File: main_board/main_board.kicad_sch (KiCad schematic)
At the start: 74 parts, among them J2 Conn_01x02, J3 Conn_01x02, J4 EncSide, J5 MainSide, J6 EncSide, J7 MainSide, Q1 ST-1KL3A, Q2 ST-1KL3A, Q3 ST-1KL3A, Q4 ST-1KL3A, Q5 IRLML6344, Q6 IRLML6344, Q7 IRLML6344, Q8 IRLML6344, U1 ADCS7476, U10 AS5047D, U11 LSM6DSR, U2 BD63573NUV, U3 ADCS7476, U4 ADCS7476, U5 BD63573NUV, U6 ESP32-S3-PICO-1-N8R2, U7 AS5047D, U8 ADCS7476, U9 ADCS7476

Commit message: アートワーク : 部品配置
Signed-off-by: Kazuki Iida <elkel53930@gmail.com>
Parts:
- D4, D5: footprint Library:SFH4550 -> Library:SFH4550_Mirror
- Q1, Q2: footprint Library:ST-1KL3A -> Library:ST-1KL3A_Mirror
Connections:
- net CS_ENC_L: now also U6.40 (GPIO35); no longer U6.24 (GPIO18)
- net CS_ENC_R: now also U6.41 (GPIO36); no longer U6.25 (GPIO19)
- net CWCCW_L: now also U6.39 (GPIO34); no longer U6.40 (GPIO35)
- net CWCCW_R: now also U6.43 (GPIO38); no longer U6.42 (GPIO37)
- net LED_0: now also R1.1; no longer R1.2
- net LED_1: now also U6.24 (GPIO18); no longer U6.38 (GPIO33)
- net PWM_L: now also U6.38 (GPIO33); no longer U6.39 (GPIO34)
- net PWM_R: now also U6.42 (GPIO37); no longer U6.41 (GPIO36)
- net at D1.1 (K): now also R1.2; no longer R1.1
- net RXD renamed RXD0
- net TXD renamed TXD0
- no-connect marks 35 -> 38
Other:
- moved on the sheet: R1
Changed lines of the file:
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@@
 	)
 	(no_connect
+		(at 218.44 99.06)
+	)
+	(no_connect
 		(at 379.73 171.45)
 	)
@@
 	)
 	(no_connect
+		(at 233.68 154.94)
+	)
+	(no_connect
 		(at 379.73 203.2)
 	)
@@
 	)
 	(no_connect
+		(at 223.52 154.94)
+	)
+	(no_connect
 		(at 220.98 154.94)
 	)
@@
 	(wire
 		(pts
-			(xy 218.44 83.82) (xy 218.44 99.06)
-		)
-		(stroke
-			(width 0)
-			(type default)
-		)
-	)
-	(wire
-		(pts
 			(xy 85.09 172.72) (xy 96.52 172.72)
 		)
@@
 	(wire
 		(pts
+			(xy 171.45 118.11) (xy 185.42 118.11)
+		)
+		(stroke
+			(width 0)
+			(type default)
+		)
+	)
+	(wire
+		(pts
 			(xy 226.06 255.27) (xy 226.06 252.73)
 		)
@@
 	(wire
 		(pts
-			(xy 231.14 154.94) (xy 231.14 170.18)
-		)
-		(stroke
-			(width 0)
-			(type default)
-		)
-	)
-	(wire
-		(pts
 			(xy 45.72 107.95) (xy 49.53 107.95)
 		)
@@
 	(wire
 		(pts
+			(xy 238.76 83.82) (xy 238.76 99.06)
+		)
+		(stroke
+			(width 0)
+			(type default)
+		)
+	)
+	(wire
+		(pts
 			(xy 68.58 149.86) (xy 60.96 149.86)
 		)
@@
 	(wire
 		(pts
-			(xy 115.57 96.52) (xy 115.57 92.71)
+			(xy 171.45 120.65) (xy 194.31 120.65)
 		)
 		(stroke
@@
 	(wire
 		(pts
-			(xy 179.07 120.65) (xy 194.31 120.65)
+			(xy 115.57 96.52) (xy 115.57 92.71)
 		)
 		(stroke
@@
 	(wire
 		(pts
-			(xy 179.07 118.11) (xy 185.42 118.11)
-		)
-		(stroke
-			(width 0)
-			(type default)
-		)
-	)
-	(wire
-		(pts
 			(xy 322.58 125.73) (xy 325.12 125.73)
 		)
@@
 	(wire
 		(pts
-			(xy 233.68 154.94) (xy 233.68 170.18)
-		)
-		(stroke
-			(width 0)
-			(type default)
-		)
-	)
-	(wire
-		(pts
 			(xy 250.19 115.57) (xy 265.43 115.57)
 		)
@@
 		)
 	)
-	(label "CHIP_PU"
-		(at 179.07 118.11 180)
-		(effects
-			(font
-				(size 1.27 1.27)
-			)
-			(justify right bottom)
-		)
-	)
 	(label "CS_RS"
 		(at 179.07 125.73 180)
@@
 	)
 	(label "CS_ENC_L"
-		(at 228.6 170.18 270)
+		(at 265.43 115.57 0)
 		(effects
 			(font
 				(size 1.27 1.27)
 			)
-			(justify right bottom)
+			(justify left bottom)
 		)
 	)
@@
 		)
 	)
-	(label "TXD"
-		(at 223.52 83.82 90)
-		(effects
-			(font
-				(size 1.27 1.27)
-			)
-			(justify left bottom)
-		)
-	)
 	(label "CS_IMU"
 		(at 226.06 219.71 90)
@@
 		)
 	)
-	(label "RXD"
-		(at 220.98 83.82 90)
-		(effects
-			(font
-				(size 1.27 1.27)
-			)
-			(justify left bottom)
-		)
-	)
 	(label "PWM_R"
-		(at 265.43 113.03 0)
+		(at 265.43 110.49 0)
 		(effects
 			(font
@@
 	)
 	(label "LED_1"
-		(at 265.43 120.65 0)
+		(at 228.6 170.18 270)
 		(effects
 			(font
 				(size 1.27 1.27)
 			)
-			(justify left bottom)
+			(justify right bottom)
 		)
 	)
@@
 	)
 	(label "CS_ENC_R"
-		(at 231.14 170.18 270)
+		(at 265.43 113.03 0)
 		(effects
 			(font
 				(size 1.27 1.27)
 			)
-			(justify right bottom)
+			(justify left bottom)
 		)
 	)
@@
 	)
 	(label "PWM_L"
-		(at 265.43 118.11 0)
+		(at 265.43 120.65 0)
 		(effects
 			(font
@@
 	)
 	(label "CWCCW_L"
-		(at 265.43 115.57 0)
+		(at 265.43 118.11 0)
 		(effects
 			(font
@@
 	)
 	(label "CWCCW_R"
-		(at 265.43 110.49 0)
+		(at 238.76 83.82 90)
 		(effects
 			(font
@@
 		)
 	)
-	(label "GPIO0"
-		(at 179.07 120.65 180)
-		(effects
-			(font
-				(size 1.27 1.27)
-			)
-			(justify right bottom)
-		)
-	)
 	(label "PWM_R"
 		(at 314.96 72.39 180)
@@
 		)
 	)
+	(global_label "RXD0"
+		(shape input)
+		(at 220.98 83.82 90)
+		(fields_autoplaced yes)
+		(effects
+			(font
+				(size 1.27 1.27)
+			)
+			(justify left)
+		)
+		(property "Intersheetrefs" "${INTERSHEET_REFS}"
+			(at 220.98 75.8758 90)
+			(effects
+				(font
+					(size 1.27 1.27)
+				)
+				(justify left)
+				(hide yes)
+			)
+		)
+	)
+	(global_label "TXD0"
+		(shape input)
+		(at 223.52 83.82 90)
+		(fields_autoplaced yes)
+		(effects
+			(font
+				(size 1.27 1.27)
+			)
+			(justify left)
+		)
+		(property "Intersheetrefs" "${INTERSHEET_REFS}"
+			(at 223.52 76.1782 90)
+			(effects
+				(font
+					(size 1.27 1.27)
+				)
+				(justify left)
+				(hide yes)
+			)
+		)
+	)
+	(global_label "GPIO0"
+		(shape input)
+		(at 171.45 120.65 180)
+		(fields_autoplaced yes)
+		(effects
+			(font
+				(size 1.27 1.27)
+			)
+			(justify right)
+		)
+		(property "Intersheetrefs" "${INTERSHEET_REFS}"
+			(at 162.78 120.65 0)
+			(effects
+				(font
+					(size 1.27 1.27)
+				)
+				(justify right)
+				(hide yes)
+			)
+		)
+	)
+	(global_label "CHIP_PU"
+		(shape input)
+		(at 171.45 118.11 180)
+		(fields_autoplaced yes)
+		(effects
+			(font
+				(size 1.27 1.27)
+			)
+			(justify right)
+		)
+		(property "Intersheetrefs" "${INTERSHEET_REFS}"
+			(at 160.4214 118.11 0)
+			(effects
+				(font
+					(size 1.27 1.27)
+				)
+				(justify right)
+				(hide yes)
+			)
+		)
+	)
 	(symbol
 		(lib_id "micromouse:ADCS747x")
@@
 			)
 		)
-		(property "Footprint" "Library:ST-1KL3A"
+		(property "Footprint" "Library:ST-1KL3A_Mirror"
 			(at 87.63 101.6 0)
 			(effects
@@
 			)
 		)
-		(property "Footprint" "Library:ST-1KL3A"
+		(property "Footprint" "Library:ST-1KL3A_Mirror"
 			(at 40.64 101.6 0)
 			(effects
@@
 			)
 		)
-		(property "Footprint" "Library:SFH4550"
+		(property "Footprint" "Library:SFH4550_Mirror"
 			(at 69.215 222.25 0)
 			(effects
@@
 	(symbol
 		(lib_id "Device:R")
-		(at 223.52 39.37 90)
+		(at 223.52 39.37 270)
+		(mirror x)
 		(unit 1)
 		(exclude_from_sim no)
@@
 		(dnp no)
 		(property "Reference" "R1"
-			(at 224.79 41.91 90)
+			(at 222.25 41.91 90)
 			(effects
 				(font
@@
 		)
 		(property "Value" "1608 1k"
-			(at 227.33 36.83 90)
+			(at 219.71 36.83 90)
 			(effects
 				(font
@@
 			)
 		)
-		(property "Footprint" "Library:SFH4550"
+		(property "Footprint" "Library:SFH4550_Mirror"
 			(at 42.545 222.25 0)
 			(effects

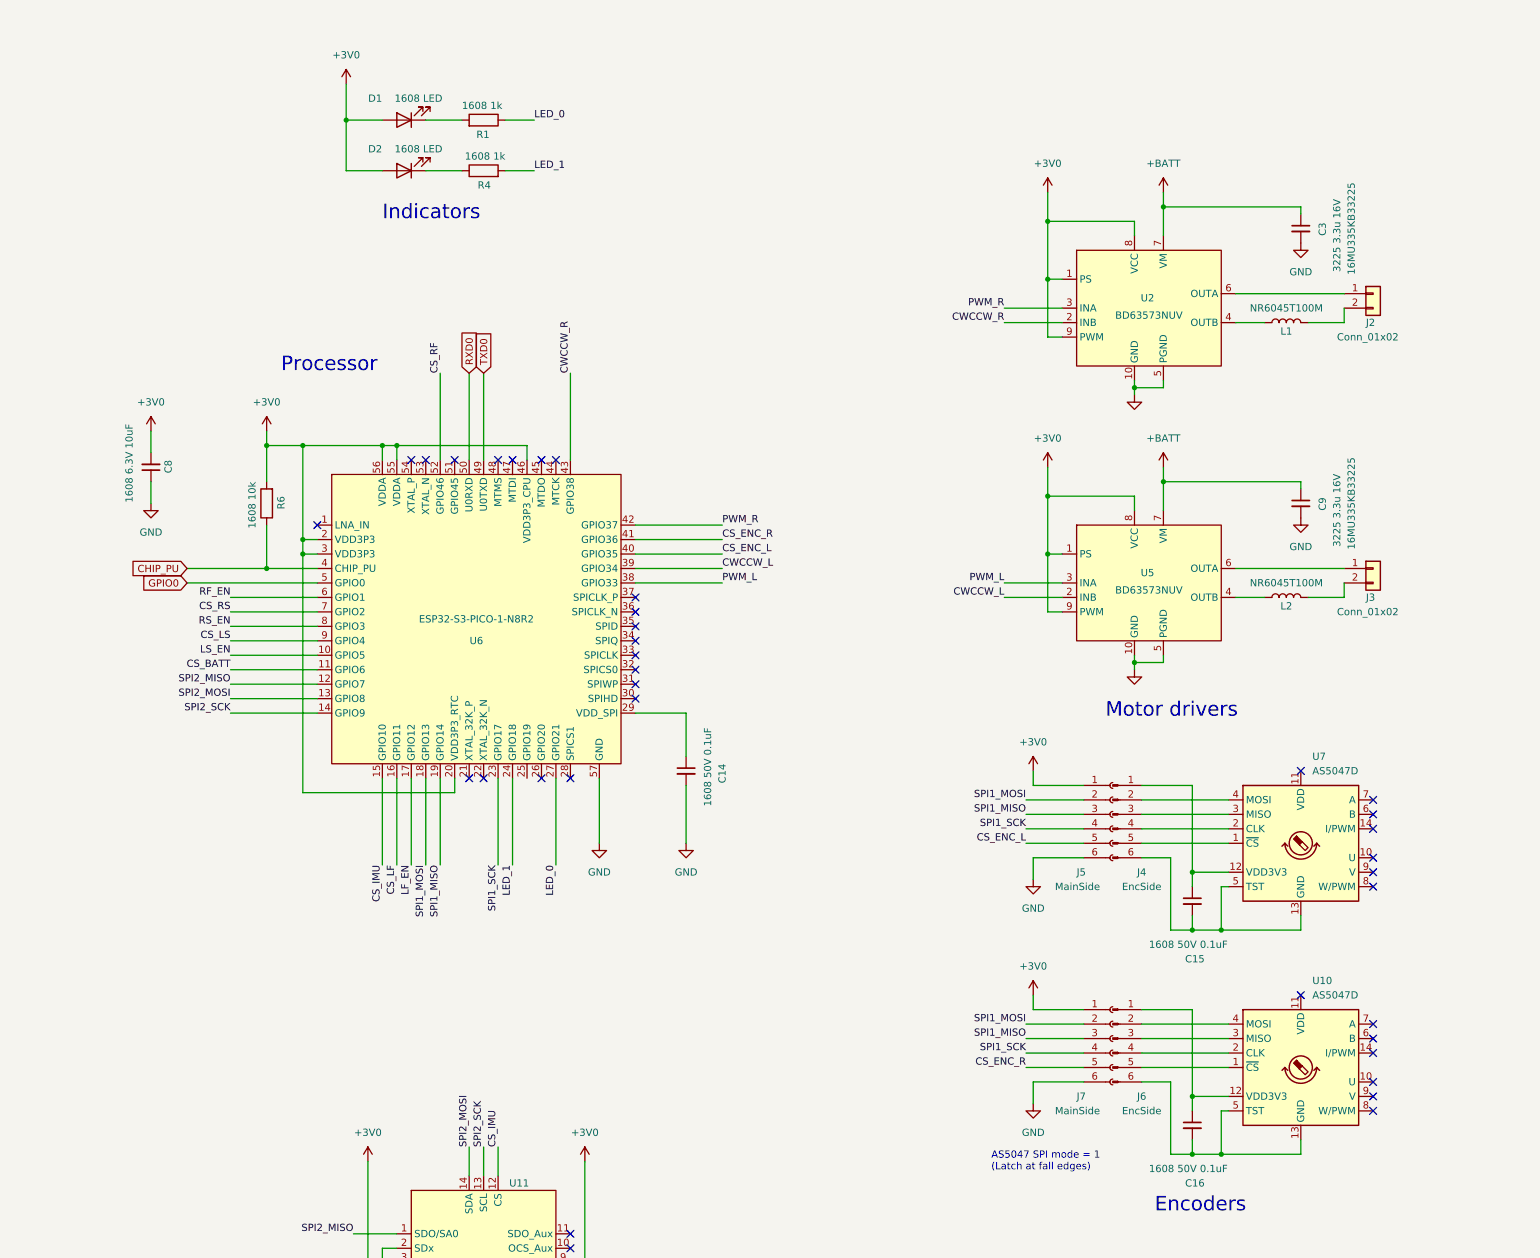
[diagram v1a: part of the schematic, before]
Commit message: アートワーク : 部品配置完了
Signed-off-by: Kazuki Iida <elkel53930@gmail.com>
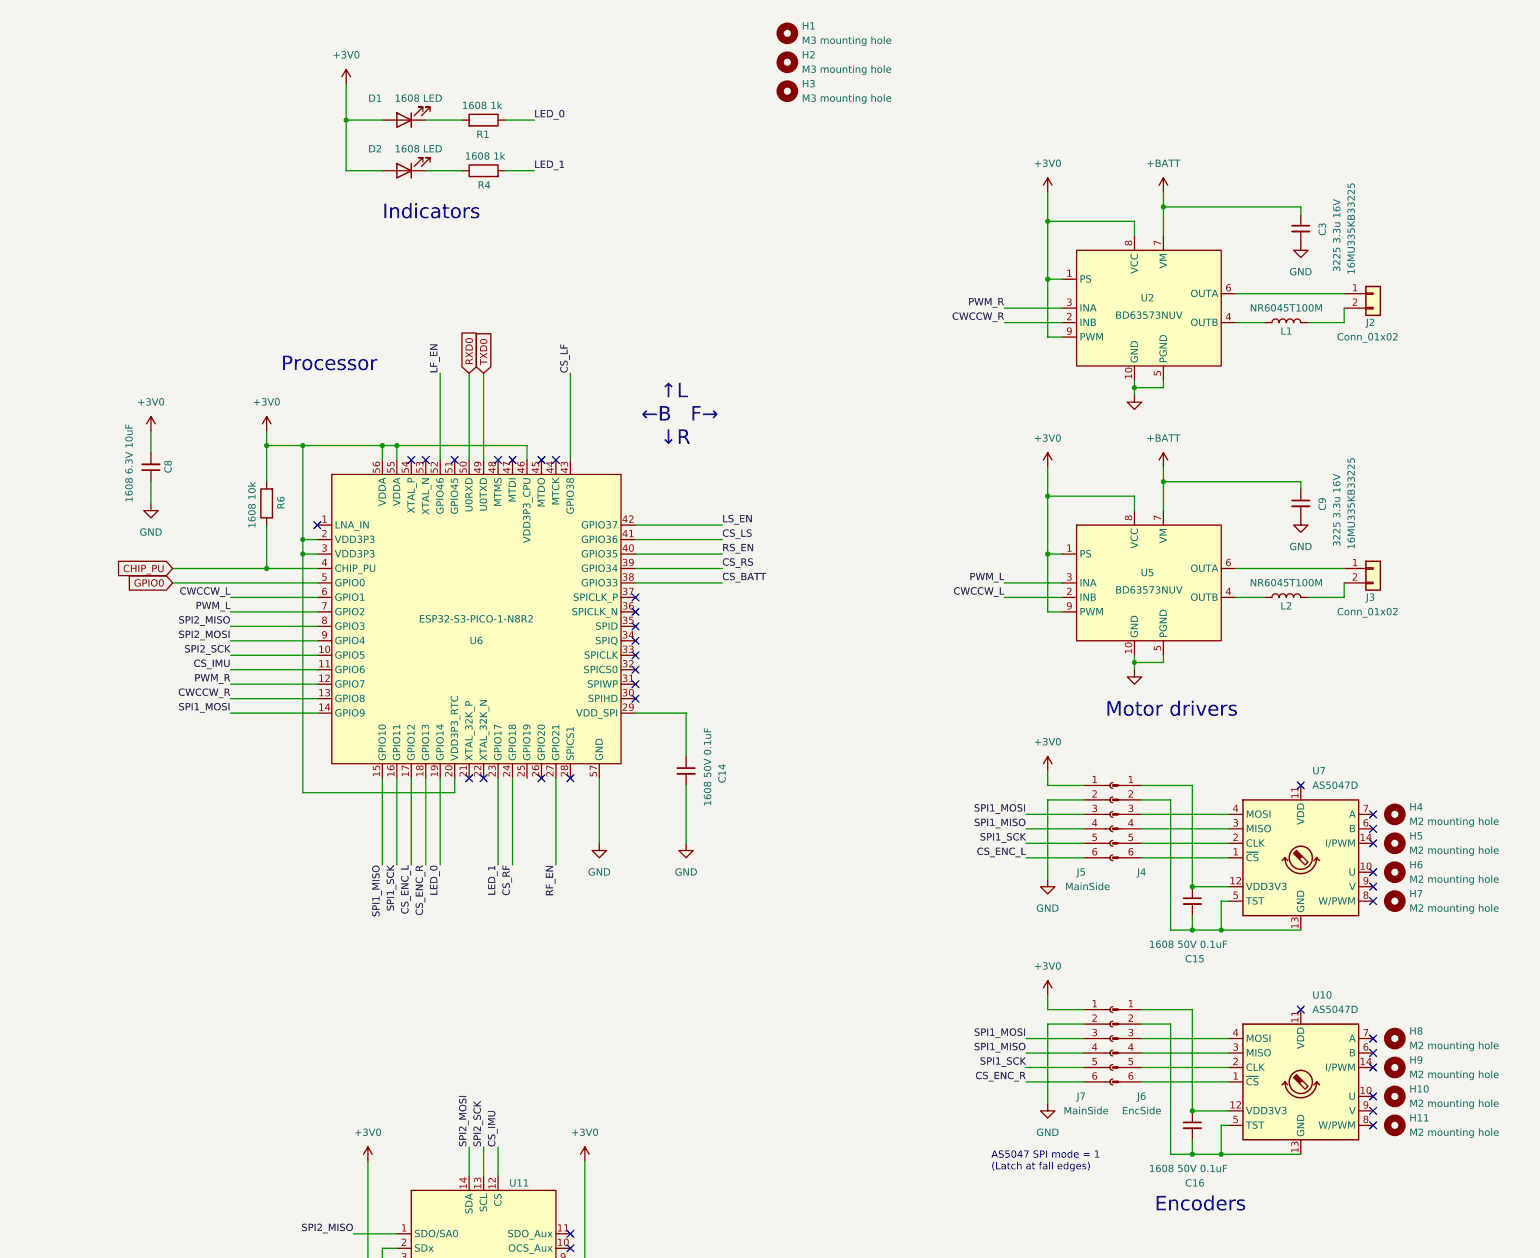
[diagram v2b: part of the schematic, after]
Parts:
- added H1, H2, H3: M3 mounting hole, MountingHole:MountingHole_3.2mm_M3, symbol Mechanical:MountingHole
- added H10, H11, H4, H5, H6, H7, H8, H9: M2 mounting hole, MountingHole:MountingHole_2.2mm_M2, symbol Mechanical:MountingHole
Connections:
- net CS_BATT: now also U6.38 (GPIO33); no longer U6.11 (GPIO6)
- net CS_ENC_L: now also J5.6 (Pin_6), U6.17 (GPIO12); no longer J5.5 (Pin_5), U6.40 (GPIO35)
- net CS_ENC_R: now also J7.6 (Pin_6), U6.18 (GPIO13); no longer J7.5 (Pin_5), U6.41 (GPIO36)
- net CS_IMU: now also U6.11 (GPIO6); no longer U6.15 (GPIO10)
- net CS_LF: now also U6.43 (GPIO38); no longer U6.16 (GPIO11)
- net CS_LS: now also U6.41 (GPIO36); no longer U6.9 (GPIO4)
- net CS_RF: now also U6.24 (GPIO18); no longer U6.52 (GPIO46)
- net CS_RS: now also U6.39 (GPIO34); no longer U6.7 (GPIO2)
- net CWCCW_L: now also U6.6 (GPIO1); no longer U6.39 (GPIO34)
- net CWCCW_R: now also U6.13 (GPIO8); no longer U6.43 (GPIO38)
- net GND: now also J5.2 (Pin_2), J7.2 (Pin_2); no longer J5.6 (Pin_6), J7.6 (Pin_6)
- net LED_0: now also U6.19 (GPIO14); no longer U6.27 (GPIO21)
- net LED_1: now also U6.23 (GPIO17); no longer U6.24 (GPIO18)
- net LF_EN: now also U6.52 (GPIO46); no longer U6.17 (GPIO12)
- net LS_EN: now also U6.42 (GPIO37); no longer U6.10 (GPIO5)
- net PWM_L: now also U6.7 (GPIO2); no longer U6.38 (GPIO33)
- net PWM_R: now also U6.12 (GPIO7); no longer U6.42 (GPIO37)
- net RF_EN: now also U6.27 (GPIO21); no longer U6.6 (GPIO1)
- net RS_EN: now also U6.40 (GPIO35); no longer U6.8 (GPIO3)
- net SPI1_MISO: now also J5.4 (Pin_4), J7.4 (Pin_4), U6.15 (GPIO10); no longer J5.3 (Pin_3), J7.3 (Pin_3), U6.19 (GPIO14)
- net SPI1_MOSI: now also J5.3 (Pin_3), J7.3 (Pin_3), U6.14 (GPIO9); no longer J5.2 (Pin_2), J7.2 (Pin_2), U6.18 (GPIO13)
- net SPI1_SCK: now also J5.5 (Pin_5), J7.5 (Pin_5), U6.16 (GPIO11); no longer J5.4 (Pin_4), J7.4 (Pin_4), U6.23 (GPIO17)
- net SPI2_MISO: now also U6.8 (GPIO3); no longer U6.12 (GPIO7)
- net SPI2_MOSI: now also U6.9 (GPIO4); no longer U6.13 (GPIO8)
- net SPI2_SCK: now also U6.10 (GPIO5); no longer U6.14 (GPIO9)
- net at U7.1 (~{CS}): now also J4.6 (Pin_6); no longer J4.5 (Pin_5)
- net at C15.2, U7.13 (GND), U7.5 (TST): now also J4.2 (Pin_2); no longer J4.6 (Pin_6)
- net at U7.2 (CLK): now also J4.5 (Pin_5); no longer J4.4 (Pin_4)
- net at U7.3 (MISO): now also J4.4 (Pin_4); no longer J4.3 (Pin_3)
- net at U7.4 (MOSI): now also J4.3 (Pin_3); no longer J4.2 (Pin_2)
- net at C16.2, U10.13 (GND), U10.5 (TST): now also J6.2 (Pin_2); no longer J6.6 (Pin_6)
- net at U10.4 (MOSI): now also J6.3 (Pin_3); no longer J6.2 (Pin_2)
- net at U10.3 (MISO): now also J6.4 (Pin_4); no longer J6.3 (Pin_3)
- net at U10.2 (CLK): now also J6.5 (Pin_5); no longer J6.4 (Pin_4)
- net at U10.1 (~{CS}): now also J6.6 (Pin_6); no longer J6.5 (Pin_5)
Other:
- note added: "↑L ←B F→ ↓R"
- moved on the sheet: U10, U7

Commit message: アートワーク : 配線完了
Signed-off-by: Kazuki Iida <elkel53930@gmail.com>
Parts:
- removed H5, H9: M2 mounting hole, MountingHole:MountingHole_2.2mm_M2, symbol Mechanical:MountingHole
- added C36, C37: 1608 6.3V 10uF, Capacitor_SMD:C_0603_1608Metric, symbol Device:C_Small
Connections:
- net +3V0: now also C36.2, C37.2
- net CS_ENC_L: now also U6.15 (GPIO10); no longer U6.17 (GPIO12)
- net CS_ENC_R: now also U6.16 (GPIO11); no longer U6.18 (GPIO13)
- net CS_RS: now also U6.40 (GPIO35); no longer U6.39 (GPIO34)
- net CWCCW_L: now also U6.7 (GPIO2); no longer U6.6 (GPIO1)
- net CWCCW_R: now also U6.18 (GPIO13); no longer U6.13 (GPIO8)
- net GND: now also C36.1, C37.1
- net PWM_L: now also U6.6 (GPIO1); no longer U6.7 (GPIO2)
- net PWM_R: now also U6.17 (GPIO12); no longer U6.12 (GPIO7)
- net RS_EN: now also U6.39 (GPIO34); no longer U6.40 (GPIO35)
- net SPI1_MISO: now also U6.13 (GPIO8); no longer U6.15 (GPIO10)
- net SPI1_MOSI: now also U6.12 (GPIO7); no longer U6.14 (GPIO9)
- net SPI1_SCK: now also U6.14 (GPIO9); no longer U6.16 (GPIO11)
- no-connect marks 38 -> 39
